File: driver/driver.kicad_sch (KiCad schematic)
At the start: 24 parts, among them J1 Conn_02x08_Odd_Even_Male, J2 Conn_02x08_Odd_Even_Female, J3 Conn_01x05, J4 Conn_01x03_Pin, U1 DRV8804PWP, U2 SN74HCS165DYYR

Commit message: Add missed changes.
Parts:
- added R6: 10kΩ, PCM_JLCPCB:R_0402, symbol PCM_JLCPCB-Resistors:0402,10kΩ
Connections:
- net +3V3: now also R6.2
- net FAULT: now also J1.8 (Pin_8), J2.8 (Pin_8)
- net PO: now also R6.1

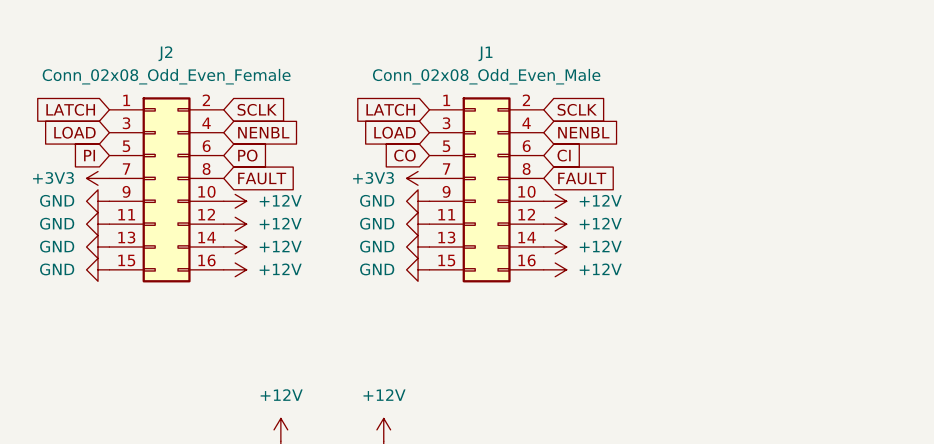
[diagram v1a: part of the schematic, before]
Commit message: Make glyph list configurable.
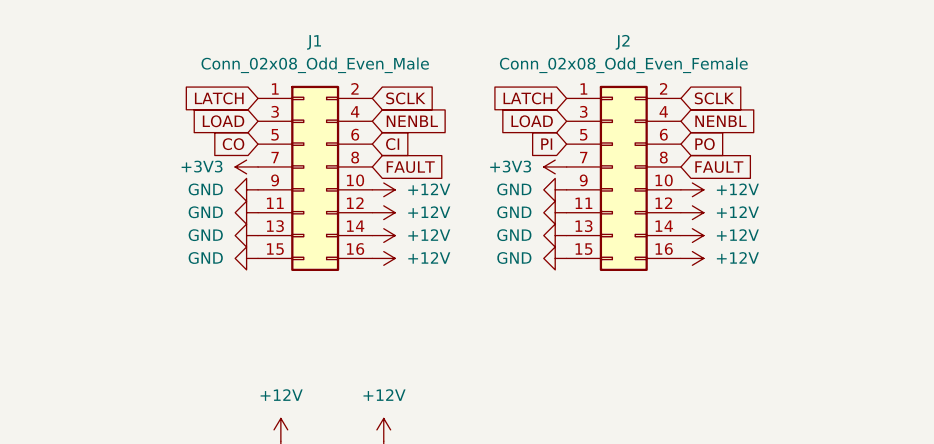
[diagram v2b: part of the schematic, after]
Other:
- moved on the sheet: J1, J2
